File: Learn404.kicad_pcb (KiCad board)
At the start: 2 copper layers, 94 x 67.3 mm, 89 parts, among them U1 LM555, U2 4520

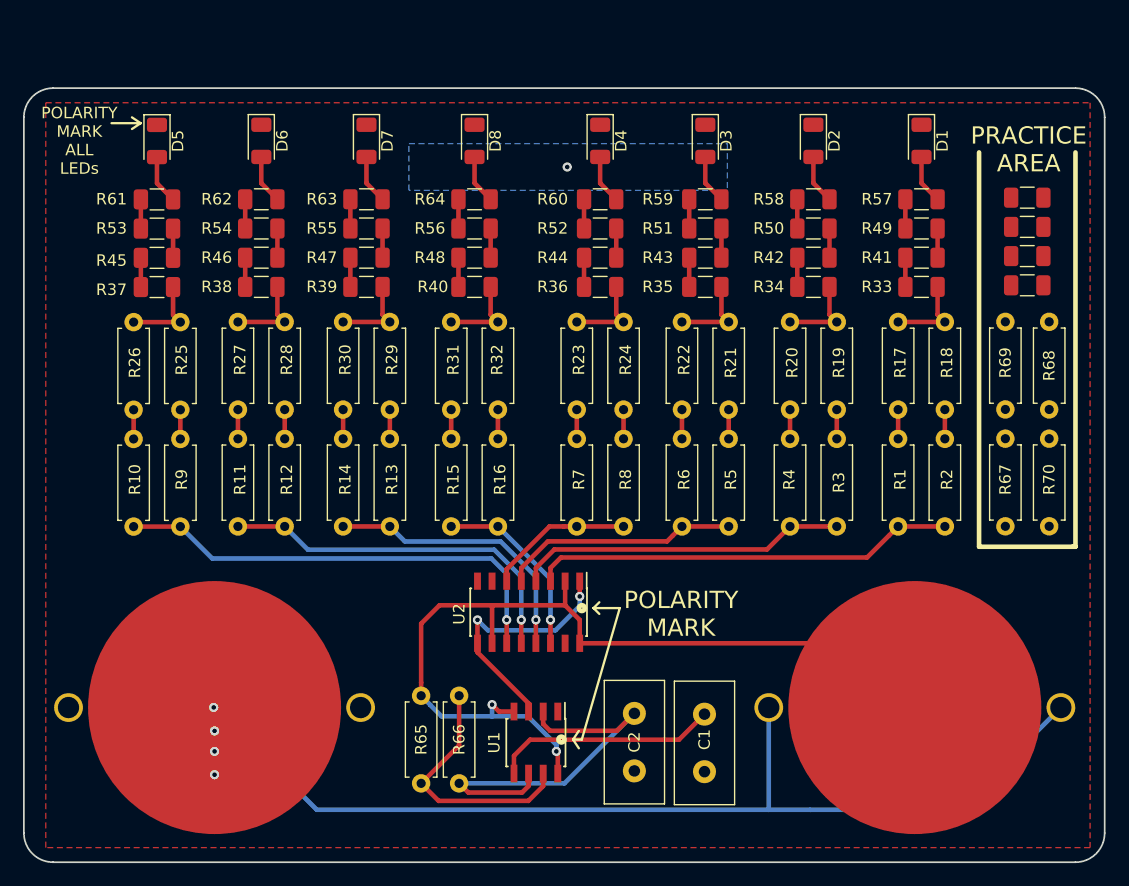
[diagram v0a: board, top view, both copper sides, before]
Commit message: Uploaded Rev B files. This board is known to work.
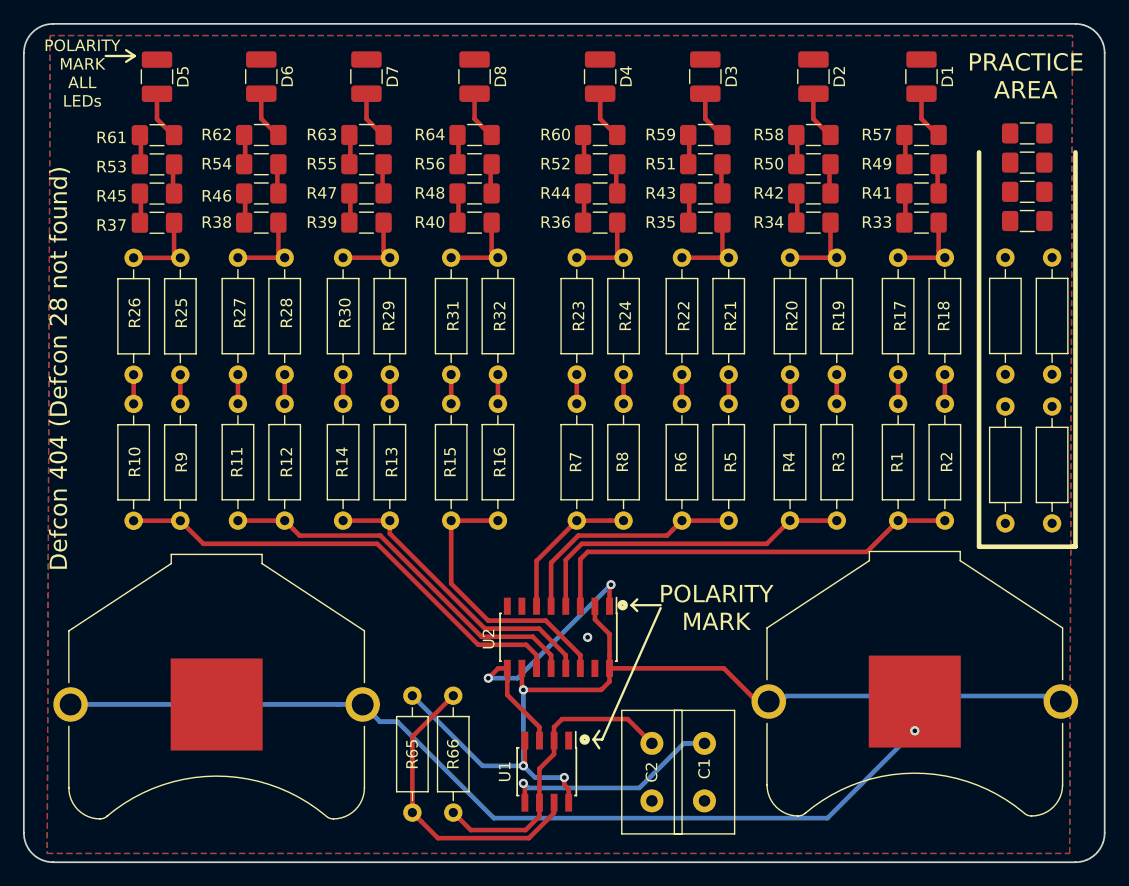
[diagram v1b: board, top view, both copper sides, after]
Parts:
- removed REF**: OSHW-Logo2_14.6x12mm_Copper, Symbol:OSHW-Logo2_14.6x12mm_Copper
- BT1, BT2: value Battery_Cell -> 3V 1000mAh; footprint Battery:3039 -> Battery:BatteryHolder_Keystone_3009_1x2450
- D1, D2, D3, D4, D5, D6, D7, D8: footprint LED_SMD:LED_1206_3216Metric -> Resistor_SMD:R_1210_3225Metric_Pad1.42x2.65mm_HandSolder
- R1, R10, R11, R12, R13, R14, R15, R16, R17, R18, R19, R2, R20, R21, R22, R23, R24, R25, R26, R27, R28, R29, R3, R30, R31, R32, R4, R5, R6, R65, R66, R67, R68, R69, R7, R70, R8, R9: footprint Resistor_THT:R_Axial_DIN0207_L6.3mm_D2.5mm_P7.62mm_Horizontal -> Resistor_THT:R_Axial_DIN0207_L6.3mm_D2.5mm_P10.16mm_Horizontal
- R33, R34, R35, R36, R37, R38, R39, R40, R41, R42, R43, R44, R45, R46, R47, R48, R49, R50, R51, R52, R53, R54, R55, R56, R57, R58, R59, R60, R61, R62, R63, R64, R71, R72, R73, R74: footprint Resistor_SMD:R_1206_3216Metric -> Resistor_SMD:R_1206_3216Metric_Pad1.42x1.75mm_HandSolder
- moved R37 5.59 mm to (99.2, 67.6)
- moved R41 5.59 mm to (165.7, 65.0)
- moved R42 5.59 mm to (156.3, 65.0)
- moved R43 5.59 mm to (146.9, 65.0)
- moved R44 5.59 mm to (137.7, 65.0)
- moved R46 5.59 mm to (108.3, 65.0)
- moved R47 5.59 mm to (117.4, 65.0)
- moved R48 5.59 mm to (126.8, 65.0)
- moved R57 5.59 mm to (165.7, 60.0)
- moved R58 5.59 mm to (156.3, 60.0)
- moved R59 5.59 mm to (146.9, 60.0)
- moved R60 5.59 mm to (137.7, 60.0)
- moved R62 5.59 mm to (108.3, 60.0)
- moved R63 5.59 mm to (117.4, 60.0)
- moved R64 5.59 mm to (126.8, 60.0)
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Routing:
- net Net-(BT1-Pad2): track 101.5 -> 80.6 mm, vias 4 -> 1
- net Net-(C2-Pad1): track 35.8 -> 26.6 mm
- net Out2D: track 16.1 -> 24.5 mm, vias 1 -> 0
- net Net-(R65-Pad1): track 22.3 -> 26.7 mm
- net Net-(U1-Pad3): track 22.6 -> 25.4 mm
- net VCC: track 83.5 -> 86.2 mm, vias 2 -> 3
- net Out2C: track 24.4 -> 26.0 mm, vias 1 -> 0
- net Out2B: track 32.2 -> 33.2 mm, vias 1 -> 0
- net Out2A: track 40.2 -> 41.0 mm, vias 1 -> 0
- net Net-(C1-Pad1): track 19.6 -> 19.3 mm, vias 0 -> 1
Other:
- board size 94 x 67.3 mm -> 94 x 72.9 mm
- board text added: "Defcon 404 (Defcon 28 not found)"
- board text added: "For more info and source files go to: https://github.com/seeigecannon/DC404TrainingBadge Twitter: DC_EnterpriseBadge"
- board text added: "You should also test the board before soldering the battery holders on by installing the battery holders and just holding them in place."
